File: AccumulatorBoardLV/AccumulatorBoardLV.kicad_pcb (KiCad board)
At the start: 2 copper layers, 157.5 x 74.9 mm, 51 parts, among them J1 Contactor 1, J10 To HV Board, J11 IMD Reset, J12 TS Interlock, J13 Temp Reset, J14 To ECU, J15 Charger LV, J16 Charger Interlock, J17 Lid Interlock, J18 From HV Board, J19 Chip 1, J2 BMS Connector 1, J20 Chip 2, J21 Chip 3, J22 Chip 4, J3 BMS Connector 2, J4 BMS TX, J5 BMS RX, J6 Current Sensor, J7 Contactor 2, J8 IMD LV, J9 BMS Reset, U1 DE1A1B-L2-12V, U10 MCP3008, U11 ISO1050, U12 stm_nucleo_FK303K8, U13 MCP3008, U14 MCP3008, U2 LM555N, U3 SN754410, U4 DE1A1B-L2-12V, U5 L78S05CV-DG, U6 DE1A1B-L2-12V, U7 DK1A1B-12V, U8 ADUM4154ARIZ, U9 MCP3008

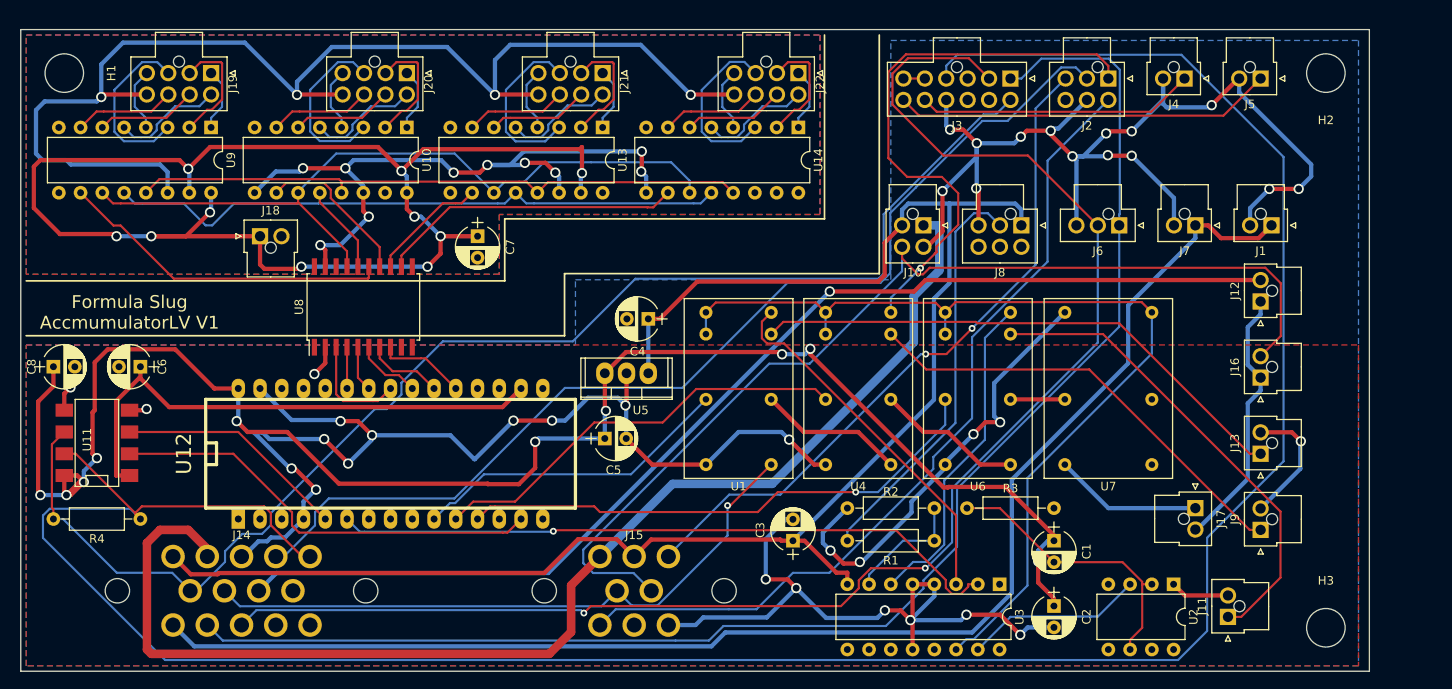
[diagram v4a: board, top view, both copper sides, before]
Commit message: Tweak silkscreen labels on boards for final run
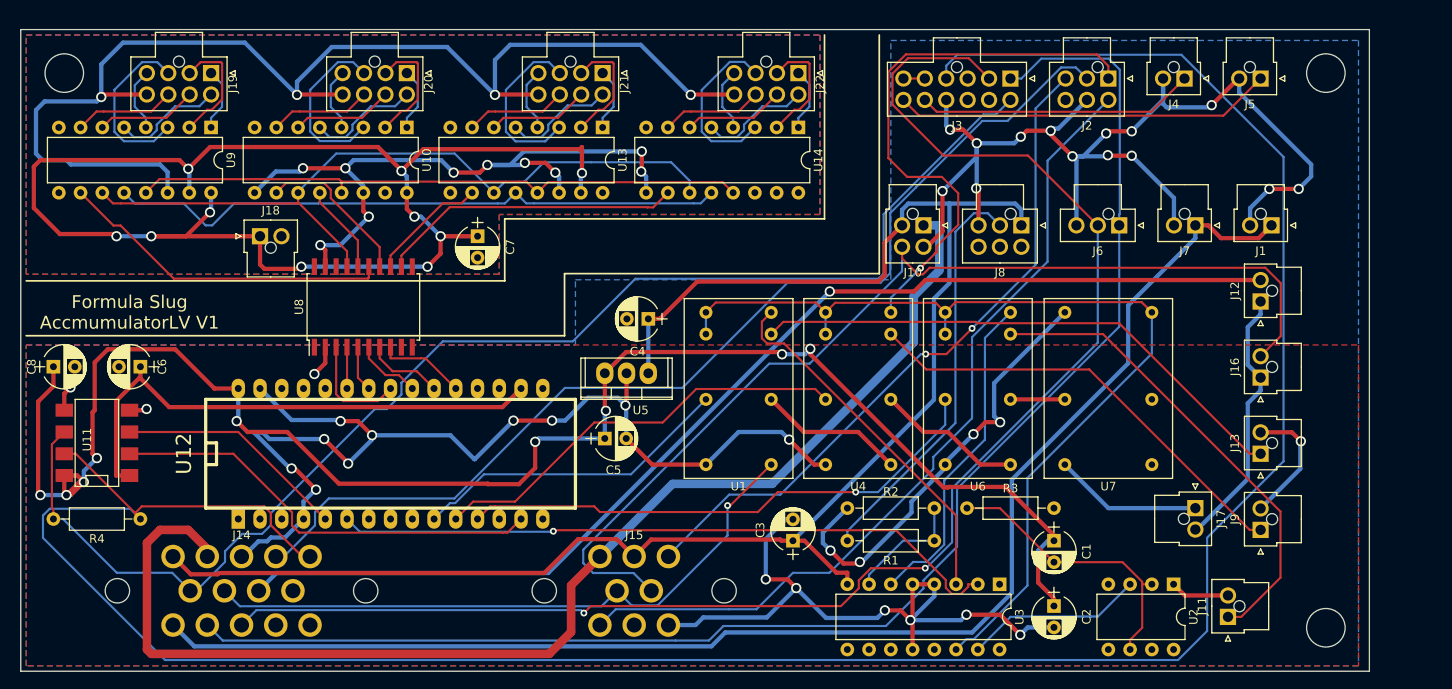
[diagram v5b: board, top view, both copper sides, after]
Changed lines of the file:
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@@
     (visible_elements 7FFFFFFF)
     (pcbplotparams
-      (layerselection 0x000fc_80000001)
+      (layerselection 0x010fc_80000001)
       (usegerberextensions false)
       (excludeedgelayer true)
@@
       (drillshape 0)
       (scaleselection 1)
-      (outputdirectory C:/Users/Nicky/FS/fs-1-schematics/AccumulatorBoardJoined/PCB/))
+      (outputdirectory PCB/))
   )
   (net 0 "")
@@
     (tags "mounting hole 4.5mm no annular")
     (attr virtual)
-    (fp_text reference H3 (at 0 -5.5) (layer F.SilkS)
+    (fp_text reference H3 (at 0 -5.5) (layer F.SilkS) hide
       (effects (font (size 1 1) (thickness 0.15)))
     )
@@
     (tags "mounting hole 4.5mm no annular")
     (attr virtual)
-    (fp_text reference H2 (at 0 -5.5 180) (layer F.SilkS)
+    (fp_text reference H2 (at 0 -5.5 180) (layer F.SilkS) hide
       (effects (font (size 1 1) (thickness 0.15)))
     )
@@
     (tags "mounting hole 4.5mm no annular")
     (attr virtual)
-    (fp_text reference H1 (at 0 -5.5 270) (layer F.SilkS)
+    (fp_text reference H1 (at 0 -5.5 270) (layer F.SilkS) hide
       (effects (font (size 1 1) (thickness 0.15)))
     )
@@
   (segment (start 165.227 151.5934) (end 156.6254 151.5934) (width 0.25) (layer B.Cu) (net 60))
   (segment (start 145.415 145.2245) (end 144.4625 145.2245) (width 0.25) (layer B.Cu) (net 61))
-  (segment (start 144.4625 145.2245) (end 141.859 147.828) (width 0.25) (layer B.Cu) (net 61) (status 800000))
+  (segment (start 144.4625 145.2245) (end 141.859 147.828) (width 0.25) (layer B.Cu) (net 61))
   (segment (start 146.0703 145.2245) (end 145.415 145.2245) (width 0.25) (layer B.Cu) (net 61))
   (segment (start 148.09 143.2048) (end 146.0703 145.2245) (width 0.25) (layer B.Cu) (net 61))

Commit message: Revise boards based on design review
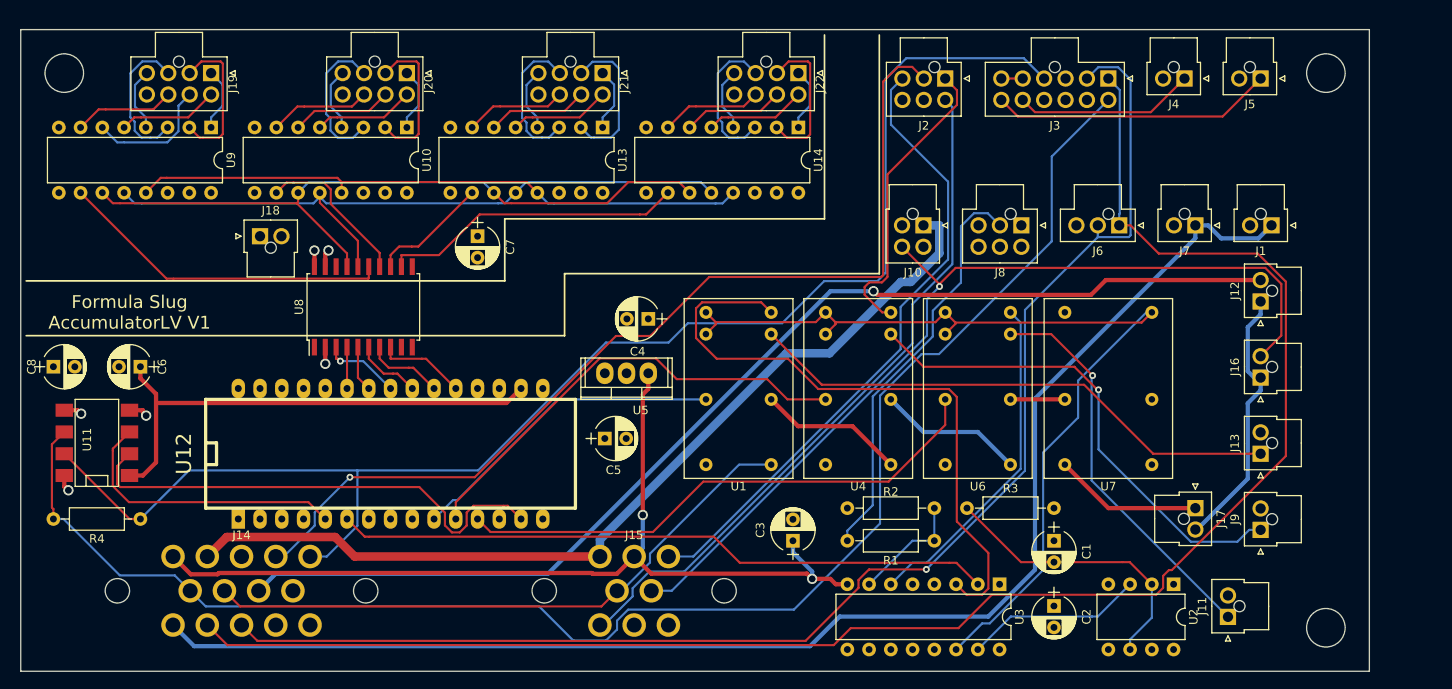
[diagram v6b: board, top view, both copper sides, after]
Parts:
- moved J2 19.0 mm to (148.2, 88.8)
- moved J3 11.4 mm to (167.3, 88.8)
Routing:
- net GND: track 417.2 -> 6.43 mm, vias 38 -> 3
- net /BATT-: track 223.1 -> 2.05 mm, vias 14 -> 1
- net +5V: track 198.7 -> 1.97 mm, vias 10 -> 1
- net /3.3V_TS: track 161.0 -> 1.89 mm, vias 10 -> 1
- net /CAN_H: track 299.6 -> 167.6 mm
- net +12V: track 193.7 -> 115.1 mm, vias 0 -> 2
- net /12V_SRC: track 146.7 -> 108.3 mm
- net /TEMP_FLT_H: track 42.8 -> 74.8 mm
- net /BMS_FLT: track 65.9 -> 35.1 mm, vias 1 -> 0
- net /5V_BMS: track 171.2 -> 197.2 mm
- net /CAN_L: track 156.2 -> 181.2 mm
- net /SIG_CURRENT: track 178.3 -> 161.5 mm, vias 2 -> 1
- net /CHARGER_CONTROL: track 98.0 -> 81.4 mm
- net /AIRS_FINAL_CHARGER: track 121.3 -> 108.2 mm, vias 0 -> 1
- net /BMS_TX: track 32.5 -> 21.1 mm
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- added copper zone on In1.Cu, net +12V
- added copper zone on In1.Cu, net +5V
- added copper zone on In1.Cu, net /3.3V_TS
- added copper zone on In2.Cu, net /BATT-
- added copper zone on In2.Cu, net GND
- removed copper zone on F.Cu, net +5V
- removed copper zone on F.Cu, net /3.3V_TS
- removed copper zone on B.Cu, net /BATT-
- removed copper zone on B.Cu, net GND
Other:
- copper layers 2 -> 4
- net class Default: clearance 0.2 -> 0.25
- net class HighSpeed: clearance 0.2 -> 0.25
- rule trace_clearance: 0.2 -> 0.25
- board text added: "Formula Slug AccumulatorLV V1"
- board text removed: "Formula Slug AccmumulatorLV V1"

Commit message: Add connections to connectors on PE and Acc LV boards
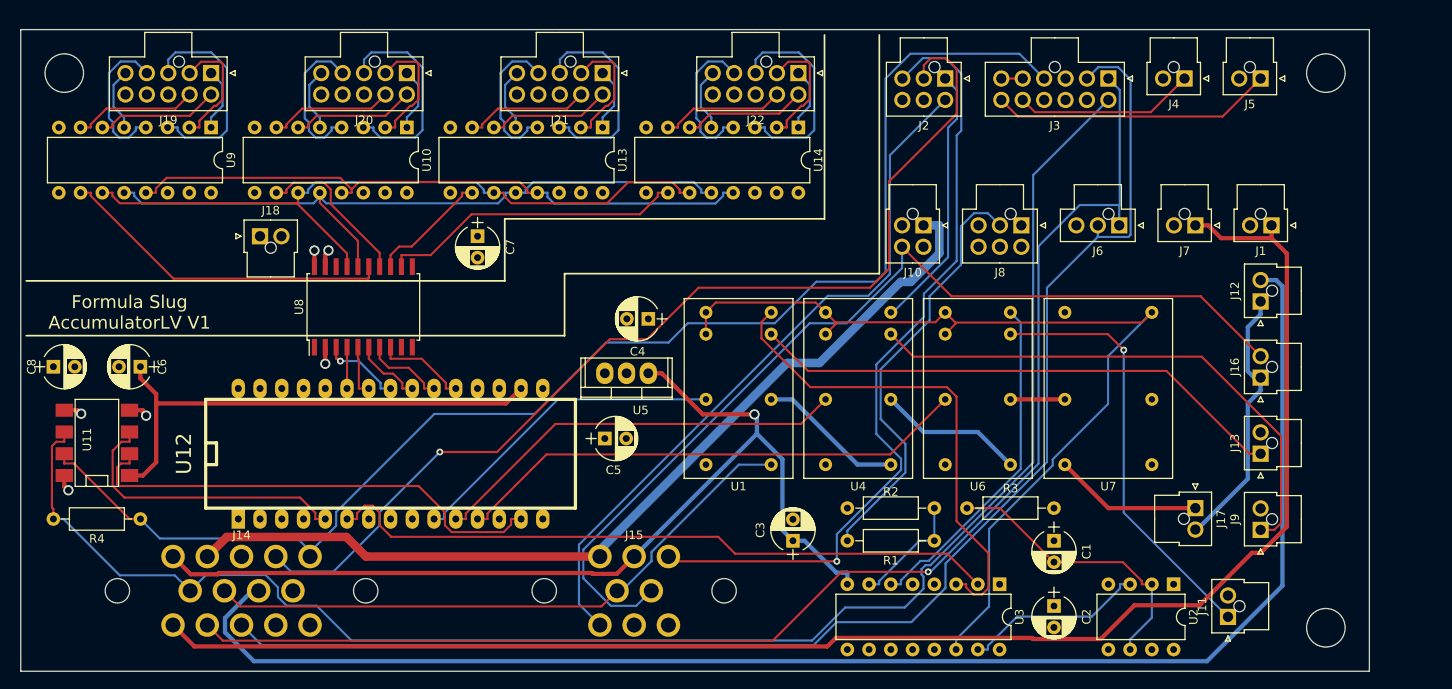
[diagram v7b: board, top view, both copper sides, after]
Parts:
- J19, J20, J21, J22: footprint Connectors_Molex:Molex_NanoFit_2x04x2.50mm_Straight -> Connectors_Molex:Molex_NanoFit_2x05x2.50mm_Straight
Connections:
- J19 pad 8: /BATT- -> (no net)
- J20 pad 8: /BATT- -> (no net)
- J21 pad 8: /BATT- -> (no net)
- J22 pad 8: /BATT- -> (no net)
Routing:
- net /AIRS_ACC_OUT: track 132.4 -> 173.3 mm, vias 1 -> 0
- net /5V_BMS: track 197.2 -> 160.9 mm, vias 0 -> 1
- net /V_S: track 74.4 -> 93.9 mm, vias 0 -> 1
- net /AIRS_FINAL: track 163.5 -> 182.4 mm
- net /TEMP_FLT_H: track 74.8 -> 57.8 mm
- net Net-(J19-Pad4): track 7.45 -> 17.4 mm
- net Net-(J22-Pad4): track 7.45 -> 17.4 mm
- net Net-(J21-Pad4): track 7.45 -> 17.4 mm
- net Net-(J20-Pad4): track 7.44 -> 17.3 mm
- net /CAN_L: track 181.2 -> 190.1 mm
- net /CAN_H: track 167.6 -> 159.9 mm
- net Net-(J22-Pad3): track 17.1 -> 24.8 mm
- net Net-(J19-Pad3): track 17.1 -> 24.8 mm
- net Net-(J21-Pad3): track 17.1 -> 24.8 mm
- net Net-(J20-Pad3): track 17.2 -> 24.8 mm
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
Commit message: redo AccumulatorBoardLV for new accumulator packaging scheme
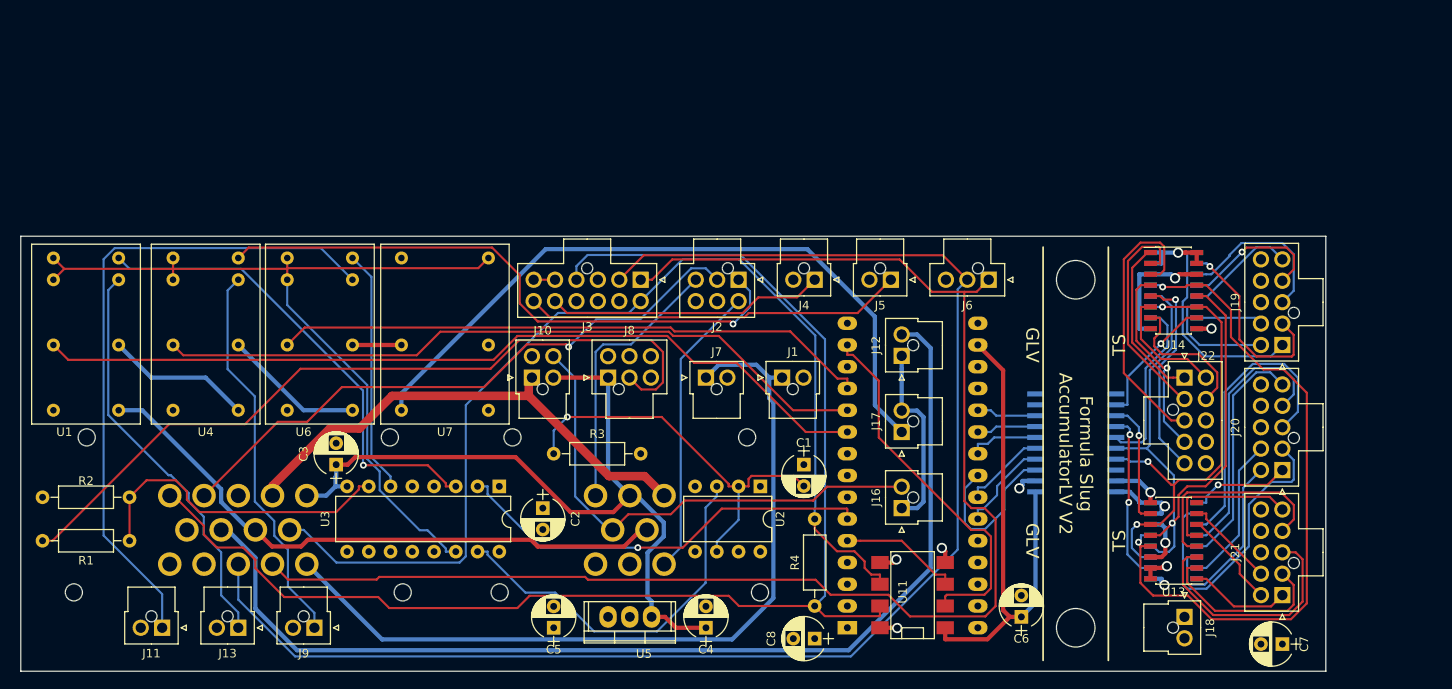
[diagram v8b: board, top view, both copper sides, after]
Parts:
- removed H3: MtngHole, Mounting_Holes:MountingHole_4.5mm
- J14: footprint FSFootprints:Ampseal - 14 pin -> FSFootprints:Ampseal-776261; moved to B.Cu
- J15: footprint FSFootprints:Ampseal - 8 pin -> FSFootprints:Ampseal-776276-1; moved to B.Cu
- U10, U9: footprint Housings_DIP:DIP-16_W7.62mm -> Housings_SOIC:SOIC-16_3.9x9.9mm_Pitch1.27mm; moved to B.Cu
- U12, U8: moved to B.Cu
- U13, U14: footprint Housings_DIP:DIP-16_W7.62mm -> Housings_SOIC:SOIC-16_3.9x9.9mm_Pitch1.27mm
- moved J19 129.1 mm to (187.6, 119.9), turned to 90 degrees
- moved J11 124.5 mm to (56.8, 152.9), turned to 180 degrees
- moved J13 121.1 mm to (65.7, 152.9), turned to 180 degrees
- moved H1 120.5 mm to (163.4, 112.3)
- moved J18 116.7 mm to (176.1, 151.6), turned to 270 degrees
- moved U9 114.0 mm to (174.9, 113.5), turned to 180 degrees
- moved J20 112.3 mm to (187.6, 134.5), turned to 90 degrees
- moved J9 111.1 mm to (74.5, 152.9), turned to 180 degrees
- moved C6 106.9 mm to (157.1, 151.6), turned to 90 degrees
- moved C7 105.4 mm to (187.6, 154.8), turned to 180 degrees
- moved U10 101.7 mm to (174.9, 142.7), turned to 180 degrees
- moved J21 100.1 mm to (187.6, 149.1), turned to 90 degrees
- moved U11 96.9 mm to (144.4, 149.1)
- moved C8 94.4 mm to (133.0, 154.2), turned to 180 degrees
- moved R2 94.0 mm to (53.0, 137.7)
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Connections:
- U8 pad 1: (no net) -> +3V3
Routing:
- net /AIRS_FINAL: track 182.4 -> 96.2 mm
- net /AIRS_RELAYS_OUT: track 17.3 -> 82.3 mm
- net /CAN_L: track 190.1 -> 125.7 mm
- net /V_S: track 93.9 -> 32.0 mm, vias 1 -> 0
- net /TEMP_FLT_LATCHED: track 37.9 -> 99.2 mm
- net /AIRS_FINAL_CHARGER: track 113.8 -> 59.3 mm
- net /12V_SRC: track 107.6 -> 58.3 mm
- net /V_L: track 120.7 -> 71.7 mm
- net /CHARGER_CONTROL: track 82.8 -> 34.3 mm
- net /AIRS_ACC_OUT: track 173.3 -> 125.9 mm
- net /IMD_FLT: track 50.4 -> 91.1 mm
- net /BMS_FLT: track 31.2 -> 70.5 mm, vias 0 -> 1
- net /BMS_FLT_LATCHED: track 49.3 -> 84.2 mm
- net +12V: track 122.0 -> 91.2 mm, vias 1 -> 0
- net /TEMP_SSI: track 84.2 -> 53.8 mm, vias 0 -> 3
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- removed copper zone on In1.Cu, net +12V
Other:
- board size 157.5 x 74.9 mm -> 152.4 x 50.8 mm
- net class Default: clearance 0.25 -> 0.24
- net class HighSpeed: clearance 0.25 -> 0.24
- rule trace_clearance: 0.25 -> 0.24
- board text added: "Formula Slug AccumulatorLV V2"
- board text added: "GLV"
- board text added: "TS"
- board text removed: "Formula Slug AccumulatorLV V1"
